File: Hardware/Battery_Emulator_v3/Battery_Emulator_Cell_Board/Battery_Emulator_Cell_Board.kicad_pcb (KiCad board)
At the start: 2 copper layers, 36.4 x 70.8 mm, 32 parts, among them J1 Conn_01x05, J3 Cell1_Vout, Q1 IRFB7545PBF, U1 LM317_TO-220, U2 ISO1640BDR, U3 MCP4651T-103E_ST, U4 KA78M05_TO252, U5 MCP6001UT-I/OT

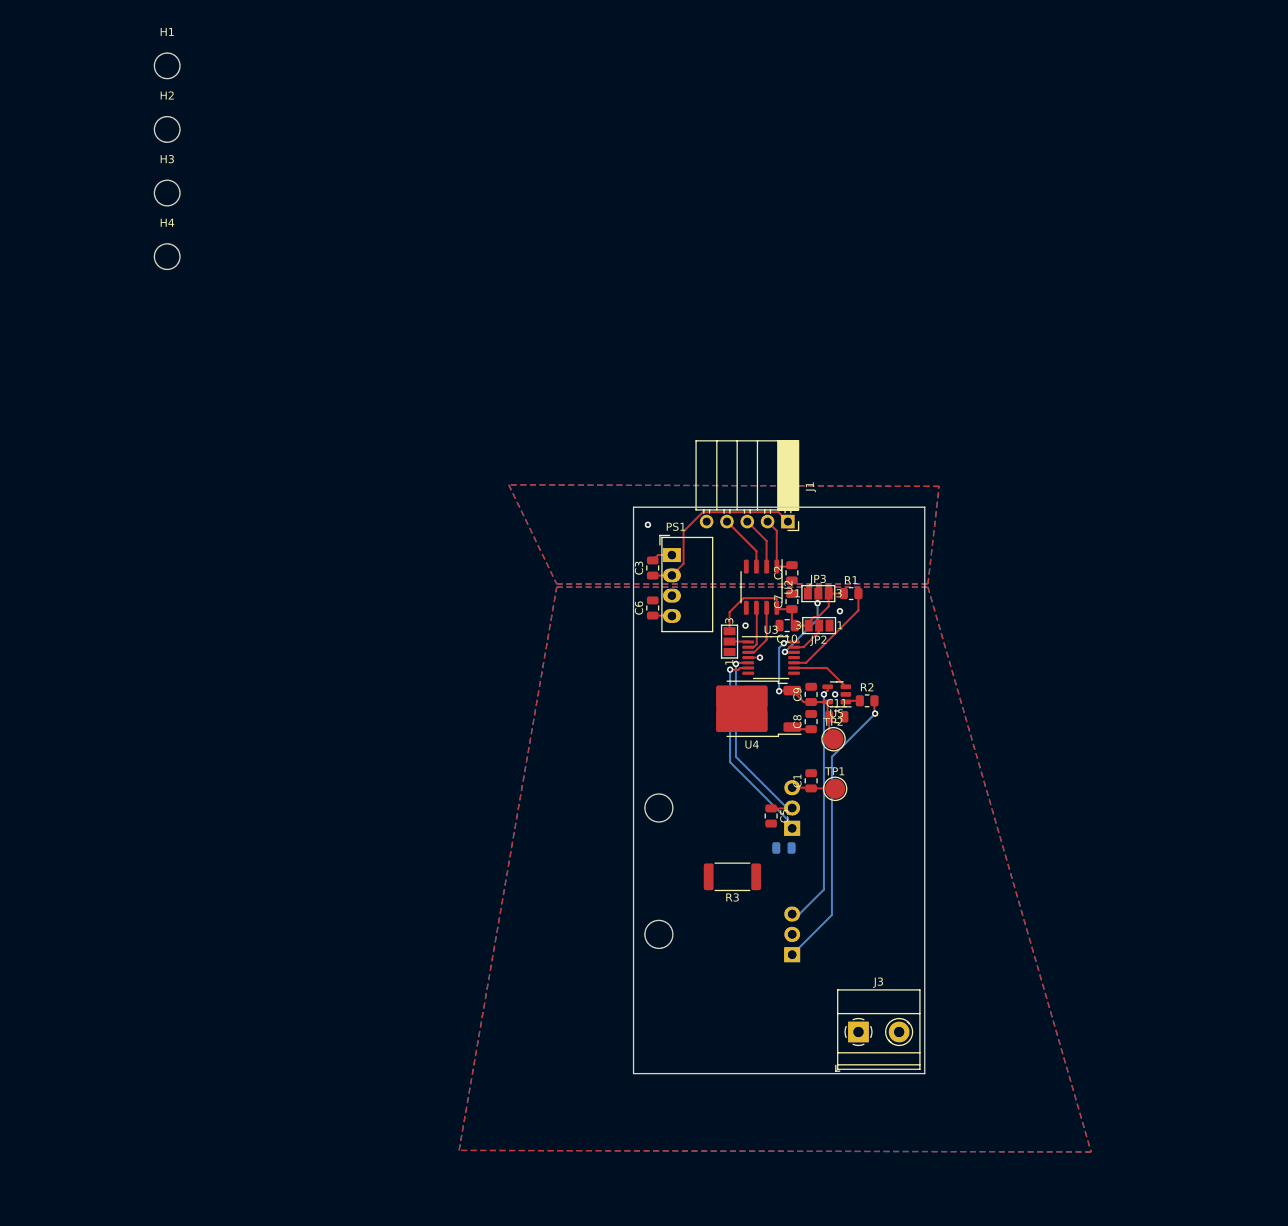
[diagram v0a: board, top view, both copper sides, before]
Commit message: Updated mother board + cell PCB
Made +12V trace on mother board 2mm so it can withstand 2A. Improved routing a bit. Changed pinheader to pinsocket on motherboard and pinsocket to pinheader on cell PCB. Mother board is nearly finished, Cell PCB is not finished.
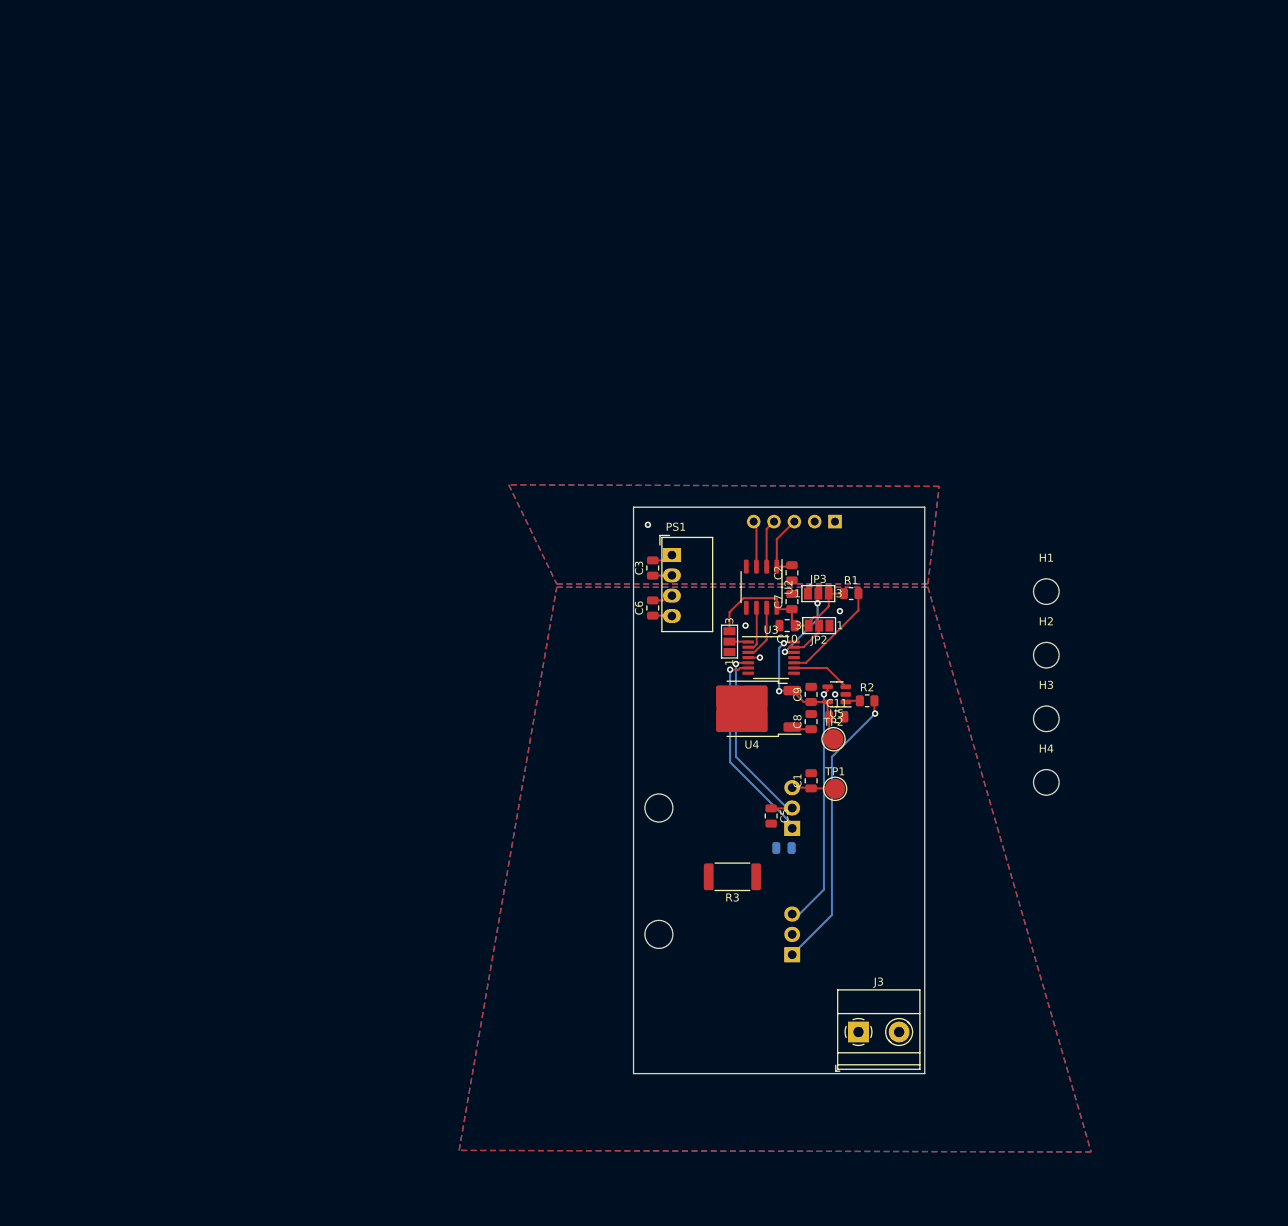
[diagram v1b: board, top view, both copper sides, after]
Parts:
- J1: footprint Connector_PinSocket_2.54mm:PinSocket_1x05_P2.54mm_Horizontal -> Connector_PinHeader_2.54mm:PinHeader_1x05_P2.54mm_Horizontal; moved to B.Cu
- moved H1 128.0 mm to (130.0, 104.2)
- moved H2 128.0 mm to (130.0, 112.1)
- moved H3 128.0 mm to (130.0, 120.0)
- moved H4 128.0 mm to (130.0, 128.0)
- moved J1 5.88 mm to (103.6, 95.4), turned to 90 degrees
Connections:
- C3 pad 2: Net-(PS1--Vin) -> /GND
- J1 pad 2: /+5V -> /GND
- J1 pad 3: /SDA -> /+5V
- J1 pad 4: /SCL -> /SDA
- J1 pad 5: /GND -> /SCL
- PS1 pad 1: Net-(PS1--Vin) -> /GND
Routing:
- net /+12V: track 23.0 -> 2.41 mm
- net Net-(PS1--Vin): track 2.68 -> 0.00 mm
- net /GND: track 0.00 -> 2.68 mm
- net /GND_ISO: track 1.46 -> 4.11 mm
- net /SCL: track 7.15 -> 5.77 mm
- net /SDA: track 6.63 -> 6.01 mm

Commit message: Updated Mother board and Cell board
Changed pinout of mother board and cell board such that the pin headers are on the top side. Finished mother board PCB and did DRC check on it.
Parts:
- J1: moved to F.Cu
- moved J1 10.2 mm to (93.4, 95.4)
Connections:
- J1 pad 1: /+12V -> /SCL
- J1 pad 2: /GND -> /SDA
- J1 pad 4: /SDA -> /GND
- J1 pad 5: /SCL -> /+12V

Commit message: Update Cell emulator PCB
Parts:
- added C12: 2u2, Capacitor_SMD:C_0805_2012Metric, F.Cu at (119.6, 92.2)
- added C13: 1n, Capacitor_SMD:C_0805_2012Metric, F.Cu at (121.6, 92.2)
- added C14: 2u2, Capacitor_SMD:C_0805_2012Metric, F.Cu at (119.8, 116.7)
- added C15: 330n, Capacitor_SMD:C_0805_2012Metric, F.Cu at (56.3, 99.8)
- added HS1: Heatsink_Pad_2Pin, Heatsink:Heatsink_AAVID_573300D00010G_TO-263, F.Cu at (119.6, 105.6)
- added HS2: Heatsink_Pad_2Pin, Heatsink:Heatsink_AAVID_573300D00010G_TO-263, F.Cu at (119.8, 129.6)
- added Q2: MJE2955T, Package_TO_SOT_THT:TO-220-3_Horizontal_TabUp, B.Cu at (106.2, 93.1)
- added Q3: MJE2955T, Package_TO_SOT_THT:TO-220-3_Horizontal_TabUp, B.Cu at (106.6, 117.1)
- added R4: 47, Resistor_SMD:R_0805_2012Metric, F.Cu at (115.6, 92.2)
- added R5: 20m, Resistor_SMD:R_2512_6332Metric, F.Cu at (103.5, 97.5)
- added R6: 47, Resistor_SMD:R_0805_2012Metric, F.Cu at (115.8, 116.7)
- added R7: 20m, Resistor_SMD:R_2512_6332Metric, F.Cu at (103.6, 122.0)
- added U6: LT3080xQ, Package_TO_SOT_SMD:TO-263-5_TabPin3, F.Cu at (119.6, 104.2)
- C1: value 100n -> 1u
- C4: value 100n -> 1u; moved to F.Cu
- C5: value 100n -> 1n
- R2: value 47 -> 10k
- U1: value LM317_TO-220 -> LT3080xQ; footprint Package_TO_SOT_THT:TO-220-3_Horizontal_TabUp -> Package_TO_SOT_SMD:TO-263-5_TabPin3; moved to F.Cu
- moved Q1 66.6 mm to (48.6, 105.0)
- moved R3 64.2 mm to (45.5, 94.2)
- moved JP3 62.7 mm to (40.7, 119.8), turned to 180 degrees
- moved JP2 61.5 mm to (40.7, 117.3)
- moved TP1 55.9 mm to (132.5, 80.9)
- moved C6 55.6 mm to (111.9, 60.1), turned to 180 degrees
- moved TP2 55.1 mm to (132.3, 75.7)
- moved C11 53.8 mm to (52.4, 104.2)
- moved R2 53.8 mm to (56.1, 102.2)
- moved U5 53.8 mm to (52.4, 101.4)
- moved C8 53.0 mm to (108.4, 68.0)
- moved C9 53.0 mm to (108.4, 64.6), turned to -90 degrees
- moved U4 53.0 mm to (101.0, 66.4)
- moved R1 52.9 mm to (54.4, 117.8), turned to 180 degrees
- moved JP1 49.9 mm to (40.7, 114.8), turned to 180 degrees
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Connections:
- C4 pad 1: Net-(U1-ADJ) -> /+9V_ISO
- C5 pad 1: Net-(J3-Pin_1) -> Net-(U1-SET)
- U1 pad 1: Net-(U1-ADJ) -> unconnected-(U1-NC-Pad1)
- U1 pad 2: Net-(J3-Pin_1) -> Net-(U1-SET)
- U1 pad 3: /+9V_ISO -> /OUT1_ISO
- U3 pad 5: Net-(J3-Pin_1) -> unconnected-(U3-P1B-Pad5)
- U3 pad 6: Net-(U1-ADJ) -> Net-(U1-SET)
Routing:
- net /+5V_ISO: track 42.5 -> 4.61 mm, vias 2 -> 0
- net Net-(C15-Pad1): track 36.1 -> 0.00 mm, vias 1 -> 0
- net Net-(U5A--): track 30.8 -> 0.00 mm, vias 1 -> 0
- net Net-(J3-Pin_1): track 25.5 -> 0.00 mm, vias 1 -> 0
- net Net-(U1-ADJ): track 25.4 -> 0.00 mm, vias 1 -> 0
- net /+9V_ISO: track 10.3 -> 29.1 mm
- net Net-(Q2-B): track 0.00 -> 17.9 mm
- net Net-(Q3-B): track 0.00 -> 17.8 mm
- net /OUT2_ISO: track 0.00 -> 15.6 mm
- net Net-(U3-P0B): track 12.9 -> 0.00 mm
- net /A2: track 10.2 -> 0.00 mm, vias 2 -> 0
- net /+12V: track 2.41 -> 11.4 mm
- net Net-(U3-P0W): track 7.45 -> 0.00 mm
- net Net-(U1-SET): track 0.00 -> 7.09 mm
- net /SDA_ISO: track 6.96 -> 0.00 mm
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- added copper zone on F.Cu, net /OUT1_ISO
- added copper zone on F.Cu, net /OUT2_ISO
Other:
- board size 36.4 x 70.8 mm -> 40 x 124.8 mm

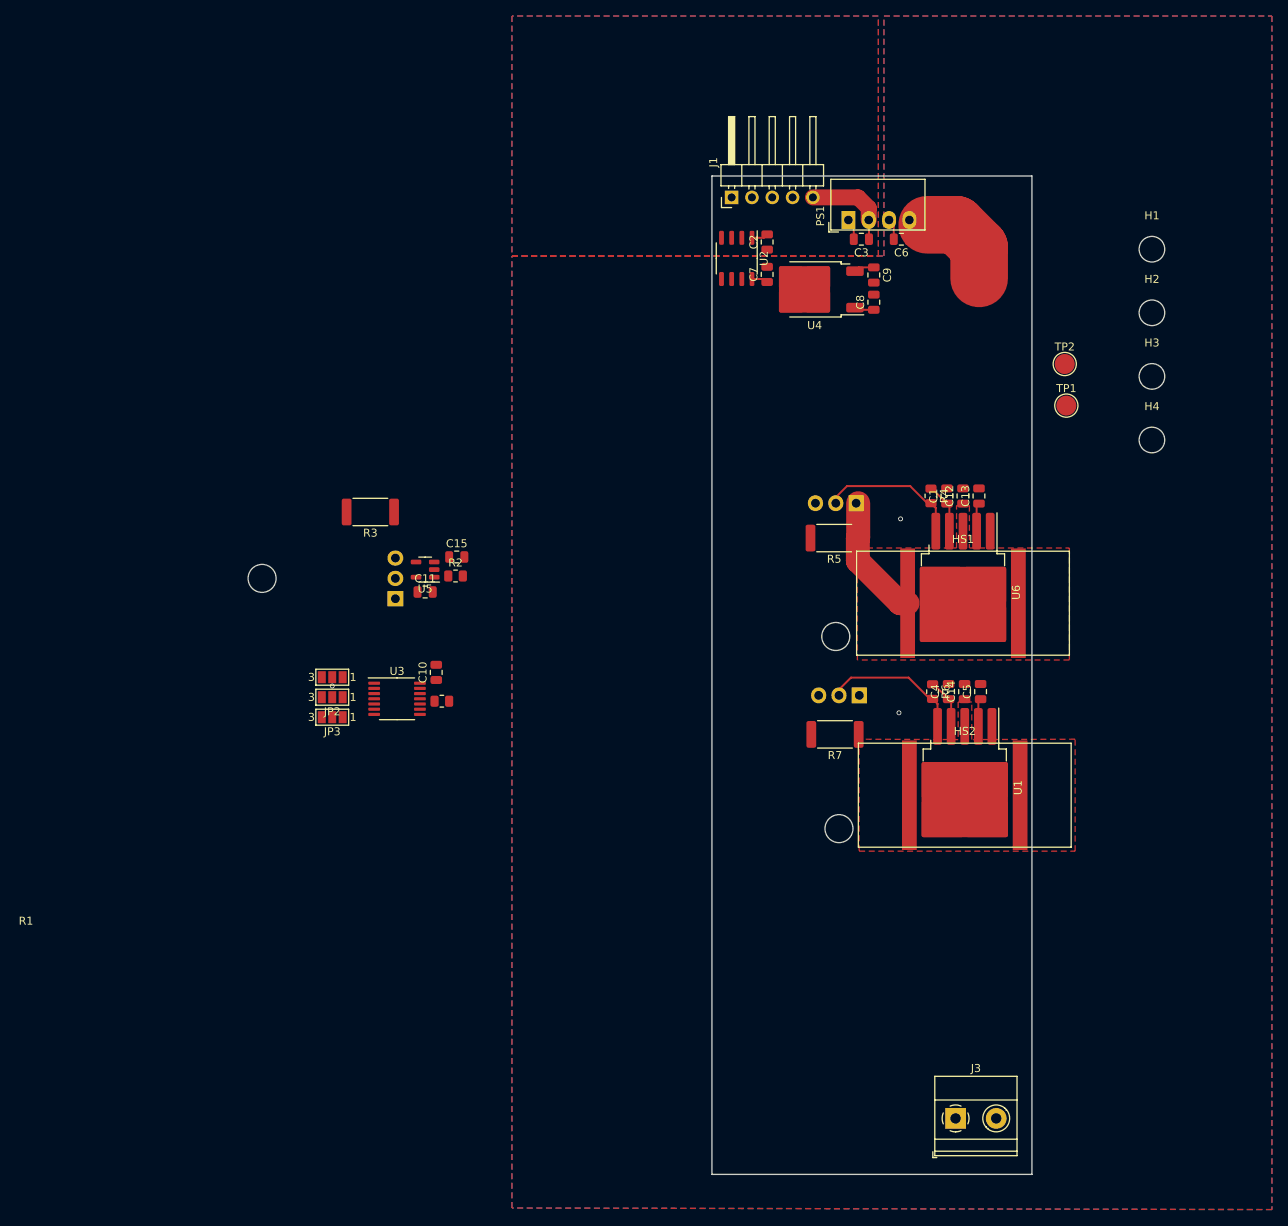
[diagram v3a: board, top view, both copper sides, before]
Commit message: Hardware Update
Updated the layout of the cell board PCB
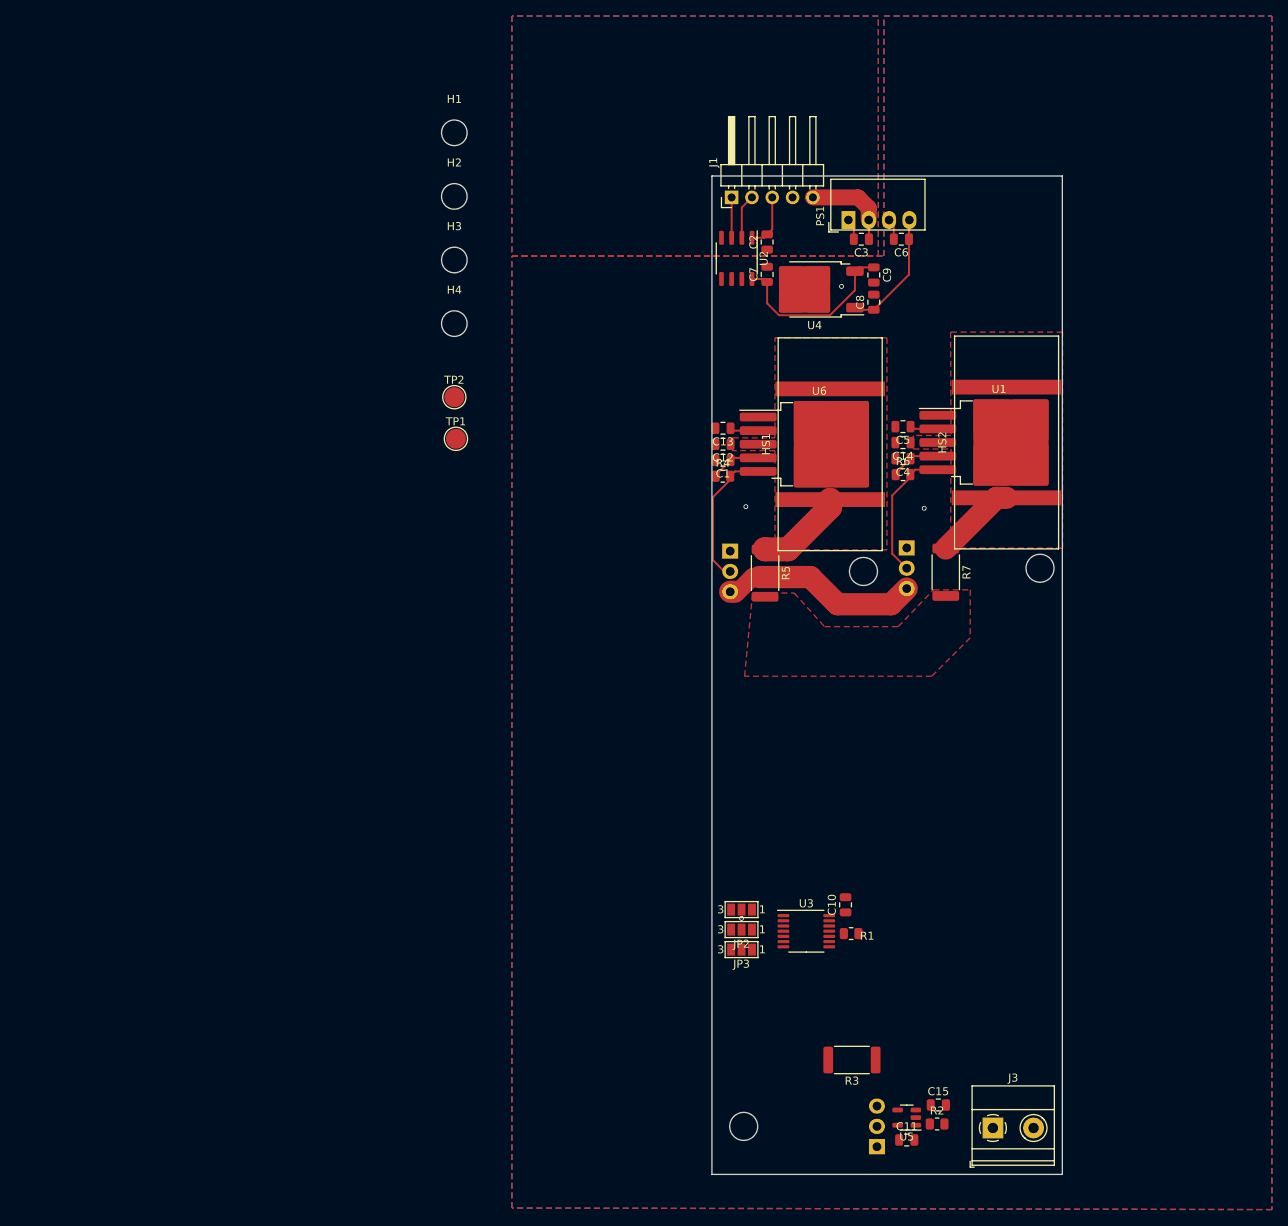
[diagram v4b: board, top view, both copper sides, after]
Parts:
- moved C15 91.2 mm to (116.5, 168.3)
- moved U5 91.2 mm to (112.5, 169.9)
- moved R3 91.2 mm to (105.7, 162.7)
- moved C11 91.2 mm to (112.5, 172.7)
- moved Q1 91.2 mm to (108.8, 173.5)
- moved R2 91.2 mm to (116.3, 170.7)
- moved H1 88.4 mm to (56.0, 46.8)
- moved H2 88.4 mm to (56.0, 54.8)
- moved H3 88.4 mm to (56.0, 62.7)
- moved H4 88.4 mm to (56.0, 70.7)
- moved TP2 76.4 mm to (56.0, 79.8)
- moved TP1 76.4 mm to (56.2, 85.0)
- moved C10 58.8 mm to (104.9, 143.3)
- moved JP1 58.8 mm to (91.9, 143.9)
- moved JP2 58.8 mm to (91.9, 146.4)
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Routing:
- net /+9V_ISO: track 29.1 -> 53.2 mm
- net /+5V_ISO: track 4.61 -> 22.5 mm
- net /OUT1_ISO: track 0.00 -> 10.2 mm
- net /SDA: track 0.00 -> 5.57 mm
- net /SCL: track 0.00 -> 5.05 mm
- net /+5V: track 2.07 -> 6.96 mm
- net /OUT2_ISO: track 15.6 -> 11.3 mm
- net Net-(Q3-B): track 17.8 -> 17.1 mm
- net /GND_ISO: vias 2 -> 3
- added copper zone on F.Cu, net Net-(J3-Pin_1)
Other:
- board size 40 x 124.8 mm -> 43.8 x 124.8 mm

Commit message: added current sink resistor
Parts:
- added R8: 56, Resistor_SMD:R_0805_2012Metric, F.Cu at (116.1, 125.0)
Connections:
- Q1 pad 1: Net-(C15-Pad1) -> Net-(Q1-Pad1)
- R2 pad 2: Net-(C15-Pad1) -> Net-(Q1-Pad1)
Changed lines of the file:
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@@
   (net 27 "unconnected-(U3-P1B-Pad5)")
   (net 28 "unconnected-(U6-NC-Pad1)")
+  (net 29 "Net-(Q1-Pad1)")
   (footprint "Resistor_SMD:R_0805_2012Metric" (layer "F.Cu")
     (at 89.56875 89.73125)
@@
       (net 17 "Net-(R2-Pad1)") (pintype "passive"))
     (pad "2" smd roundrect (at 0.9125 0) (size 1.025 1.4) (layers "F.Cu" "F.Paste" "F.Mask") (roundrect_rratio 0.243902)
-      (net 23 "Net-(C15-Pad1)") (pintype "passive"))
+      (net 29 "Net-(Q1-Pad1)") (pintype "passive"))
     (model "${KICAD6_3DMODEL_DIR}/Resistor_SMD.3dshapes/R_0805_2012Metric.wrl"
       (offset (xyz 0 0 0))
@@
       (net 1 "/+9V_ISO") (pinfunction "1") (pintype "passive"))
   )
+  (footprint "Resistor_SMD:R_0805_2012Metric" (layer "F.Cu")
+    (at 116.0875 125)
+    (descr "Resistor SMD 0805 (2012 Metric), square (rectangular) end terminal, IPC_7351 nominal, (Body size source: IPC-SM-782 page 72, https://www.pcb-3d.com/wordpress/wp-content/uploads/ipc-sm-782a_amendment_1_and_2.pdf), generated with kicad-footprint-generator")
+    (tags "resistor")
+    (property "Sheetfile" "Battery_Emulator_Cell_Board.kicad_sch")
+    (property "Sheetname" "")
+    (property "ki_description" "Resistor")
+    (property "ki_keywords" "R res resistor")
+    (attr smd)
+    (fp_text reference "R8" (at 0 -1.65) (layer "F.SilkS")
+        (effects (font (size 1 1) (thickness 0.15)))
+    )
+    (fp_text value "56" (at 0 1.65) (layer "F.Fab")
+        (effects (font (size 1 1) (thickness 0.15)))
+    )
+    (fp_text user "${REFERENCE}" (at 0 0) (layer "F.Fab")
+        (effects (font (size 0.5 0.5) (thickness 0.08)))
+    )
+    (fp_line (start -0.227064 -0.735) (end 0.227064 -0.735)
+      (stroke (width 0.12) (type solid)) (layer "F.SilkS"))
+    (fp_line (start -0.227064 0.735) (end 0.227064 0.735)
+      (stroke (width 0.12) (type solid)) (layer "F.SilkS"))
+    (fp_line (start -1.68 -0.95) (end 1.68 -0.95)
+      (stroke (width 0.05) (type solid)) (layer "F.CrtYd"))
+    (fp_line (start -1.68 0.95) (end -1.68 -0.95)
+      (stroke (width 0.05) (type solid)) (layer "F.CrtYd"))
+    (fp_line (start 1.68 -0.95) (end 1.68 0.95)
+      (stroke (width 0.05) (type solid)) (layer "F.CrtYd"))
+    (fp_line (start 1.68 0.95) (end -1.68 0.95)
+      (stroke (width 0.05) (type solid)) (layer "F.CrtYd"))
+    (fp_line (start -1 -0.625) (end 1 -0.625)
+      (stroke (width 0.1) (type solid)) (layer "F.Fab"))
+    (fp_line (start -1 0.625) (end -1 -0.625)
+      (stroke (width 0.1) (type solid)) (layer "F.Fab"))
+    (fp_line (start 1 -0.625) (end 1 0.625)
+      (stroke (width 0.1) (type solid)) (layer "F.Fab"))
+    (fp_line (start 1 0.625) (end -1 0.625)
+      (stroke (width 0.1) (type solid)) (layer "F.Fab"))
+    (pad "1" smd roundrect (at -0.9125 0) (size 1.025 1.4) (layers "F.Cu" "F.Paste" "F.Mask") (roundrect_rratio 0.243902)
+      (net 29 "Net-(Q1-Pad1)") (pintype "passive"))
+    (pad "2" smd roundrect (at 0.9125 0) (size 1.025 1.4) (layers "F.Cu" "F.Paste" "F.Mask") (roundrect_rratio 0.243902)
+      (net 23 "Net-(C15-Pad1)") (pintype "passive"))
+    (model "${KICAD6_3DMODEL_DIR}/Resistor_SMD.3dshapes/R_0805_2012Metric.wrl"
+      (offset (xyz 0 0 0))
+      (scale (xyz 1 1 1))
+      (rotate (xyz 0 0 0))
+    )
+  )
   (footprint "Package_TO_SOT_THT:TO-220-3_Horizontal_TabUp" (layer "B.Cu")
     (at 90.48125 99.09125 -90)
@@
     (pad "" np_thru_hole oval (at 2.54 -16.66 90) (size 3.5 3.5) (drill 3.5) (layers "*.Cu" "*.Mask"))
     (pad "1" thru_hole rect (at 0 0 90) (size 1.905 2) (drill 1.1) (layers "*.Cu" "*.Mask")
-      (net 23 "Net-(C15-Pad1)") (pintype "input"))
+      (net 29 "Net-(Q1-Pad1)") (pintype "input"))
     (pad "2" thru_hole oval (at 2.54 0 90) (size 1.905 2) (drill 1.1) (layers "*.Cu" "*.Mask")
       (net 7 "Net-(J3-Pin_1)") (pintype "passive"))
